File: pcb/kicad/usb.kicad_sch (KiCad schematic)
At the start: 5 parts, among them J1 USB_C_Receptacle_USB2.0, U5 USBLC6-2SC6

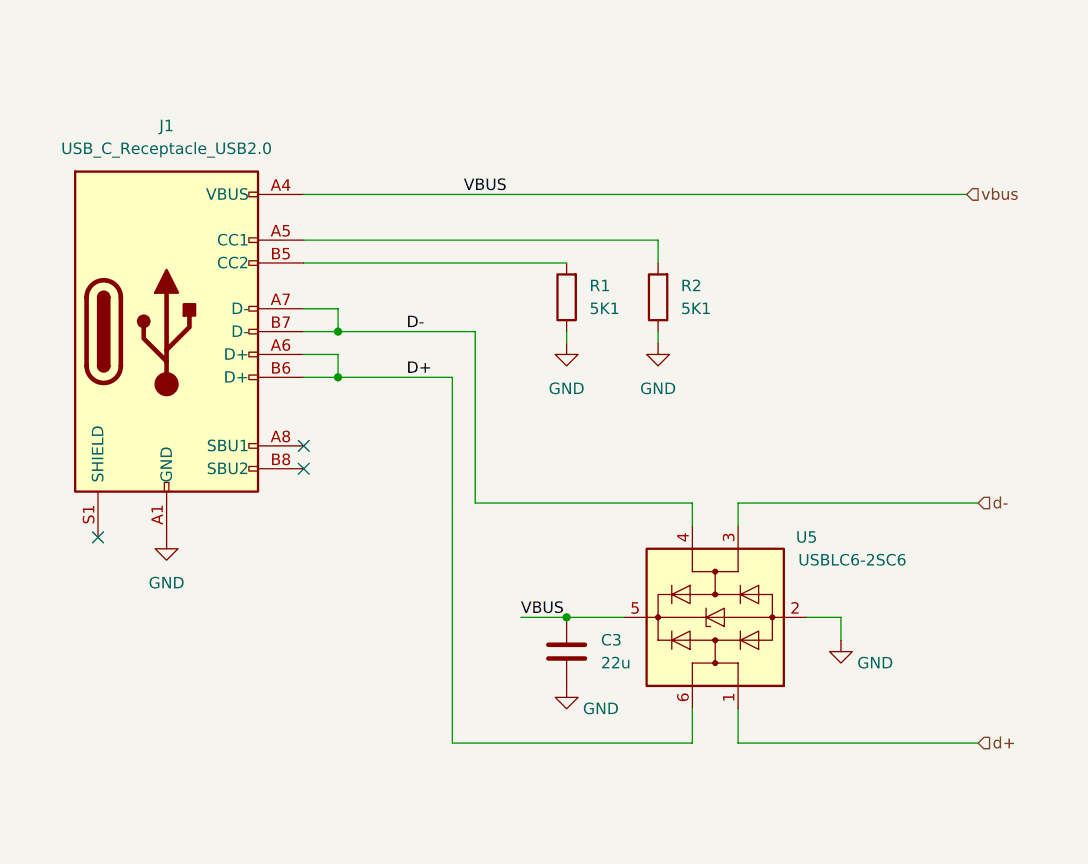
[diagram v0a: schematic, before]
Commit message: Add SoC and pinout.
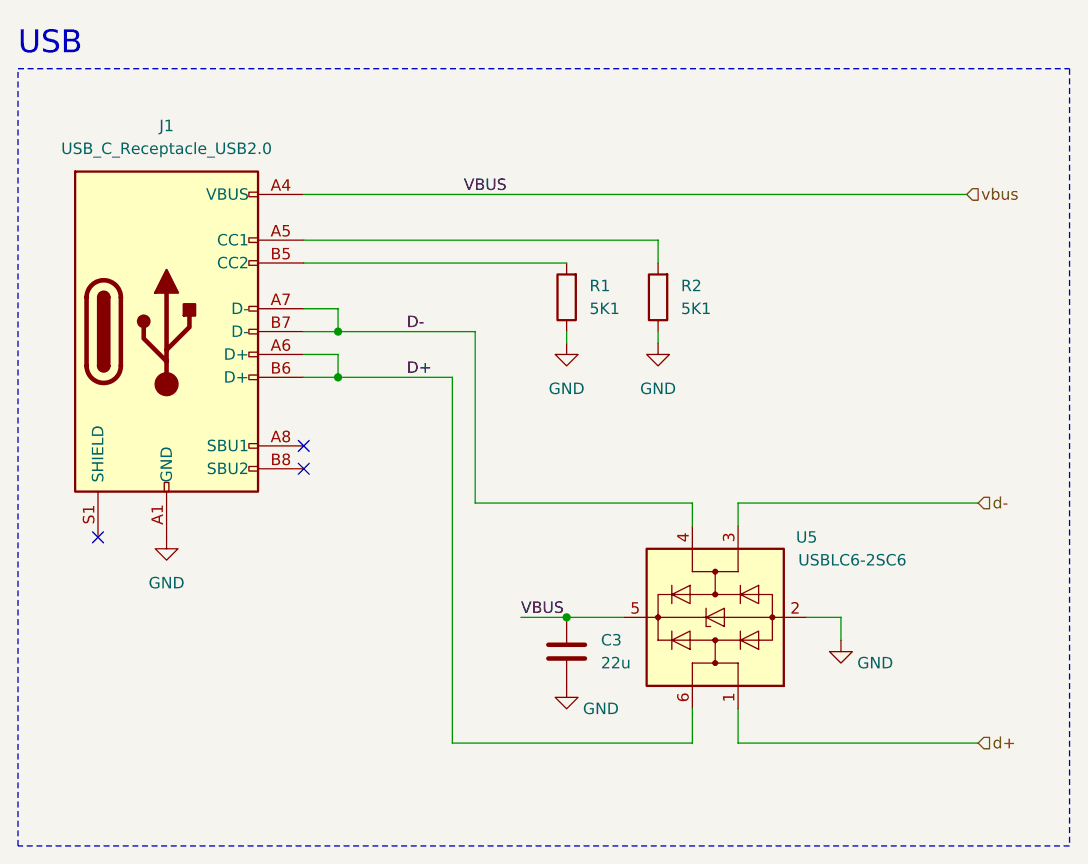
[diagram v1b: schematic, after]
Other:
- note added: "USB"
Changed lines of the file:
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@@
     (stroke (width 0) (type default))
+  )
+  (rectangle (start 88.9 55.88) (end 205.74 142.24)
+    (stroke (width 0) (type dash))
+    (fill (type none))
+  )
+  (text "USB" (at 88.9 54.61 0)
+    (effects (font (size 2.54 2.54)) (justify left bottom))
   )
   (label "D+" (at 132.08 90.17 0) (fields_autoplaced)

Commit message: Added converters, controls and updated annotations.
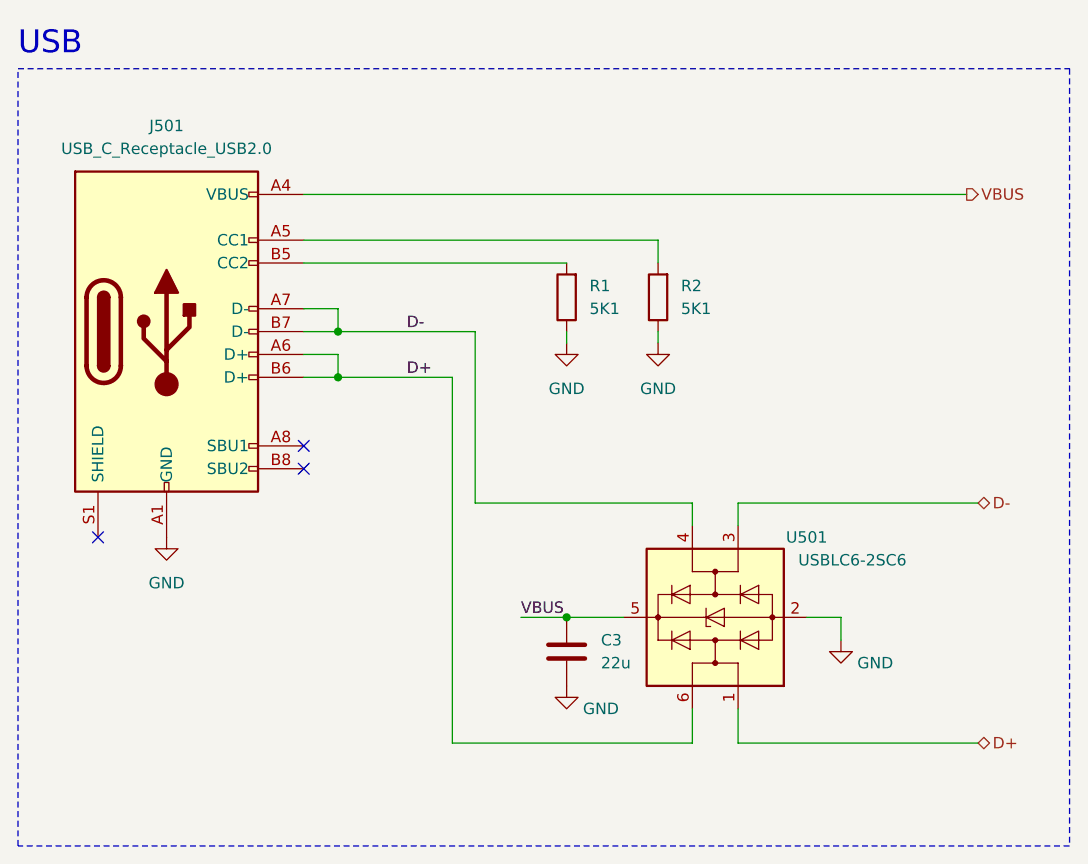
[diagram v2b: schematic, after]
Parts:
- removed J1: USB_C_Receptacle_USB2.0, symbol Connector:USB_C_Receptacle_USB2.0
- added J501: USB_C_Receptacle_USB2.0, symbol Connector:USB_C_Receptacle_USB2.0
- renumbered U5 to U501
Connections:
- net d+ is gone; now on net D+: U501.1 (I/O1)
- net d- is gone; now on net D-: U501.3 (I/O2)
- net D+: now also J501.A6 (D+), J501.B6 (D+)
- net D-: now also J501.A7 (D-), J501.B7 (D-)
- net GND: now also J501.A1 (GND), J501.A12 (GND), J501.B1 (GND), J501.B12 (GND)
- net at R2.2: now also J501.A5 (CC1)
- net at R1.2: now also J501.B5 (CC2)
- net vbus renamed VBUS
- net VBUS: now also J501.A4 (VBUS), J501.A9 (VBUS), J501.B4 (VBUS), J501.B9 (VBUS)
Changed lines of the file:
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@@
-    (effects (font (size 1.27 1.27)) (justify left bottom))
-  )
-  (label "VBUS" (at 138.43 69.85 0) (fields_autoplaced)
     (effects (font (size 1.27 1.27)) (justify left bottom))
   )
@@
     (effects (font (size 1.27 1.27)) (justify left bottom))
   )
-  (hierarchical_label "vbus" (shape input) (at 194.31 69.85 0) (fields_autoplaced)
+  (hierarchical_label "VBUS" (shape output) (at 194.31 69.85 0) (fields_autoplaced)
     (effects (font (size 1.27 1.27)) (justify left))
   )
-  (hierarchical_label "d-" (shape input) (at 195.58 104.14 0) (fields_autoplaced)
+  (hierarchical_label "D-" (shape bidirectional) (at 195.58 104.14 0) (fields_autoplaced)
     (effects (font (size 1.27 1.27)) (justify left))
   )
-  (hierarchical_label "d+" (shape input) (at 195.58 130.81 0) (fields_autoplaced)
+  (hierarchical_label "D+" (shape bidirectional) (at 195.58 130.81 0) (fields_autoplaced)
     (effects (font (size 1.27 1.27)) (justify left))
   )
-  (symbol (lib_id "Device:C") (at 149.86 120.65 0) (unit 1)
-    (in_bom yes) (on_board yes) (dnp no) (fields_autoplaced)
-    (property "Reference" "C3" (at 153.67 119.38 0)
-      (effects (font (size 1.27 1.27)) (justify left))
-    )
-    (property "Value" "22u" (at 153.67 121.92 0)
-      (effects (font (size 1.27 1.27)) (justify left))
-    )
-    (property "Footprint" "Capacitor_SMD:C_0805_2012Metric" (at 150.8252 124.46 0)
-      (effects (font (size 1.27 1.27)) hide)
-    )
-    (property "Datasheet" "~" (at 149.86 120.65 0)
-      (effects (font (size 1.27 1.27)) hide)
-    )
-    (pin "1")
-    (pin "2")
-    (instances
-      (project "guitar-pedal"
-        (path "/aeca30b5-691d-475f-a243-a02c48b6690c/87d54cf0-3e2a-4f61-ade7-69dbca04292f"
-          (reference "C3") (unit 1)
-        )
-        (path "/aeca30b5-691d-475f-a243-a02c48b6690c/59bf6d34-53a6-42d0-b8a6-f9cf82e6ba67"
-          (reference "C17") (unit 1)
-        )
-      )
-    )
-  )
-  (symbol (lib_id "power:GND") (at 180.34 119.38 0) (unit 1)
-    (in_bom yes) (on_board yes) (dnp no)
-    (property "Reference" "#PWR02" (at 180.34 125.73 0)
-      (effects (font (size 1.27 1.27)) hide)
-    )
-    (property "Value" "GND" (at 184.15 121.92 0)
-      (effects (font (size 1.27 1.27)))
-    )
-    (property "Footprint" "" (at 180.34 119.38 0)
-      (effects (font (size 1.27 1.27)) hide)
-    )
-    (property "Datasheet" "" (at 180.34 119.38 0)
-      (effects (font (size 1.27 1.27)) hide)
-    )
-    (pin "1")
-    (instances
-      (project "guitar-pedal"
-        (path "/aeca30b5-691d-475f-a243-a02c48b6690c"
-          (reference "#PWR02") (unit 1)
-        )
-        (path "/aeca30b5-691d-475f-a243-a02c48b6690c/59bf6d34-53a6-42d0-b8a6-f9cf82e6ba67"
-          (reference "#PWR024") (unit 1)
-        )
-      )
-    )
-  )
-  (symbol (lib_id "power:GND") (at 105.41 107.95 0) (unit 1)
-    (in_bom yes) (on_board yes) (dnp no) (fields_autoplaced)
-    (property "Reference" "#PWR01" (at 105.41 114.3 0)
-      (effects (font (size 1.27 1.27)) hide)
-    )
-    (property "Value" "GND" (at 105.41 113.03 0)
-      (effects (font (size 1.27 1.27)))
-    )
-    (property "Footprint" "" (at 105.41 107.95 0)
-      (effects (font (size 1.27 1.27)) hide)
-    )
-    (property "Datasheet" "" (at 105.41 107.95 0)
-      (effects (font (size 1.27 1.27)) hide)
-    )
-    (pin "1")
-    (instances
-      (project "guitar-pedal"
-        (path "/aeca30b5-691d-475f-a243-a02c48b6690c"
-          (reference "#PWR01") (unit 1)
-        )
-        (path "/aeca30b5-691d-475f-a243-a02c48b6690c/59bf6d34-53a6-42d0-b8a6-f9cf82e6ba67"
-          (reference "#PWR01") (unit 1)
-        )
-      )
-    )
-  )
   (symbol (lib_id "Connector:USB_C_Receptacle_USB2.0") (at 105.41 85.09 0) (unit 1)
     (in_bom yes) (on_board yes) (dnp no) (fields_autoplaced)
-    (property "Reference" "J1" (at 105.41 62.23 0)
+    (property "Reference" "J501" (at 105.41 62.23 0)
       (effects (font (size 1.27 1.27)))
     )
@@
     (instances
       (project "guitar-pedal"
-        (path "/aeca30b5-691d-475f-a243-a02c48b6690c"
-          (reference "J1") (unit 1)
-        )
-        (path "/aeca30b5-691d-475f-a243-a02c48b6690c/59bf6d34-53a6-42d0-b8a6-f9cf82e6ba67"
-          (reference "J1") (unit 1)
+        (path "/aeca30b5-691d-475f-a243-a02c48b6690c/59bf6d34-53a6-42d0-b8a6-f9cf82e6ba67"
+          (reference "J501") (unit 1)
+        )
+      )
+    )
+  )
+  (symbol (lib_id "Device:C") (at 149.86 120.65 0) (unit 1)
+    (in_bom yes) (on_board yes) (dnp no) (fields_autoplaced)
+    (property "Reference" "C3" (at 153.67 119.38 0)
+      (effects (font (size 1.27 1.27)) (justify left))
+    )
+    (property "Value" "22u" (at 153.67 121.92 0)
+      (effects (font (size 1.27 1.27)) (justify left))
+    )
+    (property "Footprint" "Capacitor_SMD:C_0805_2012Metric" (at 150.8252 124.46 0)
+      (effects (font (size 1.27 1.27)) hide)
+    )
+    (property "Datasheet" "~" (at 149.86 120.65 0)
+      (effects (font (size 1.27 1.27)) hide)
+    )
+    (pin "1")
+    (pin "2")
+    (instances
+      (project "guitar-pedal"
+        (path "/aeca30b5-691d-475f-a243-a02c48b6690c/87d54cf0-3e2a-4f61-ade7-69dbca04292f"
+          (reference "C3") (unit 1)
+        )
+        (path "/aeca30b5-691d-475f-a243-a02c48b6690c/59bf6d34-53a6-42d0-b8a6-f9cf82e6ba67"
+          (reference "C501") (unit 1)
+        )
+      )
+    )
+  )
+  (symbol (lib_id "power:GND") (at 180.34 119.38 0) (unit 1)
+    (in_bom yes) (on_board yes) (dnp no)
+    (property "Reference" "#PWR02" (at 180.34 125.73 0)
+      (effects (font (size 1.27 1.27)) hide)
+    )
+    (property "Value" "GND" (at 184.15 121.92 0)
+      (effects (font (size 1.27 1.27)))
+    )
+    (property "Footprint" "" (at 180.34 119.38 0)
+      (effects (font (size 1.27 1.27)) hide)
+    )
+    (property "Datasheet" "" (at 180.34 119.38 0)
+      (effects (font (size 1.27 1.27)) hide)
+    )
+    (pin "1")
+    (instances
+      (project "guitar-pedal"
+        (path "/aeca30b5-691d-475f-a243-a02c48b6690c"
+          (reference "#PWR02") (unit 1)
+        )
+        (path "/aeca30b5-691d-475f-a243-a02c48b6690c/59bf6d34-53a6-42d0-b8a6-f9cf82e6ba67"
+          (reference "#PWR0505") (unit 1)
+        )
+      )
+    )
+  )
+  (symbol (lib_id "power:GND") (at 105.41 107.95 0) (unit 1)
+    (in_bom yes) (on_board yes) (dnp no) (fields_autoplaced)
+    (property "Reference" "#PWR01" (at 105.41 114.3 0)
+      (effects (font (size 1.27 1.27)) hide)
+    )
+    (property "Value" "GND" (at 105.41 113.03 0)
+      (effects (font (size 1.27 1.27)))
+    )
+    (property "Footprint" "" (at 105.41 107.95 0)
+      (effects (font (size 1.27 1.27)) hide)
+    )
+    (property "Datasheet" "" (at 105.41 107.95 0)
+      (effects (font (size 1.27 1.27)) hide)
+    )
+    (pin "1")
+    (instances
+      (project "guitar-pedal"
+        (path "/aeca30b5-691d-475f-a243-a02c48b6690c"
+          (reference "#PWR01") (unit 1)
+        )
+        (path "/aeca30b5-691d-475f-a243-a02c48b6690c/59bf6d34-53a6-42d0-b8a6-f9cf82e6ba67"
+          (reference "#PWR0501") (unit 1)
         )
       )
@@
         )
         (path "/aeca30b5-691d-475f-a243-a02c48b6690c/59bf6d34-53a6-42d0-b8a6-f9cf82e6ba67"
-          (reference "#PWR02") (unit 1)
+          (reference "#PWR0502") (unit 1)
         )
       )
@@
         )
         (path "/aeca30b5-691d-475f-a243-a02c48b6690c/59bf6d34-53a6-42d0-b8a6-f9cf82e6ba67"
-          (reference "#PWR023") (unit 1)
+          (reference "#PWR0503") (unit 1)
         )
       )
@@
         )
         (path "/aeca30b5-691d-475f-a243-a02c48b6690c/59bf6d34-53a6-42d0-b8a6-f9cf82e6ba67"
-          (reference "#PWR03") (unit 1)
+          (reference "#PWR0504") (unit 1)
         )
       )
@@
         )
         (path "/aeca30b5-691d-475f-a243-a02c48b6690c/59bf6d34-53a6-42d0-b8a6-f9cf82e6ba67"
-          (reference "R2") (unit 1)
+          (reference "R502") (unit 1)
         )
       )
@@
   (symbol (lib_id "Power_Protection:USBLC6-2SC6") (at 166.37 116.84 90) (unit 1)
     (in_bom yes) (on_board yes) (dnp no)
-    (property "Reference" "U5" (at 176.53 107.95 90)
+    (property "Reference" "U501" (at 176.53 107.95 90)
       (effects (font (size 1.27 1.27)))
     )
@@
       (project "guitar-pedal"
         (path "/aeca30b5-691d-475f-a243-a02c48b6690c/59bf6d34-53a6-42d0-b8a6-f9cf82e6ba67"
-          (reference "U5") (unit 1)
+          (reference "U501") (unit 1)
         )
       )
@@
         )
         (path "/aeca30b5-691d-475f-a243-a02c48b6690c/59bf6d34-53a6-42d0-b8a6-f9cf82e6ba67"
-          (reference "R1") (unit 1)
-        )
-      )
+          (reference "R501") (unit 1)
+        )
+      )

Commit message: Added PCB layout and fabrication output.
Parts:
- J501: value USB_C_Receptacle_USB2.0 -> USB4105-GF-A; footprint (none) -> Connector_USB:USB_C_Receptacle_GCT_USB4105-xx-A_16P_TopMnt_Horizontal
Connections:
- net D+: no longer J501.A6 (D+), J501.B6 (D+), U501.6 (I/O1)
- net D-: no longer J501.A7 (D-), J501.B7 (D-), U501.4 (I/O2)
- new net CONN_D+: J501.A6 (D+), J501.B6 (D+), U501.6 (I/O1)
- new net CONN_D-: J501.A7 (D-), J501.B7 (D-), U501.4 (I/O2)
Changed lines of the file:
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@@
+    (stroke (width 0) (type default))
+  )
+  (wire (pts (xy 124.46 90.17) (xy 137.16 90.17))
     (stroke (width 0) (type default))
   )
@@
     (stroke (width 0) (type default))
   )
+  (wire (pts (xy 124.46 85.09) (xy 139.7 85.09))
+    (stroke (width 0) (type default))
+  )
   (wire (pts (xy 144.78 116.84) (xy 149.86 116.84))
     (stroke (width 0) (type default))
@@
     (stroke (width 0) (type default))
   )
-  (wire (pts (xy 124.46 85.09) (xy 139.7 85.09))
-    (stroke (width 0) (type default))
-  )
   (wire (pts (xy 176.53 116.84) (xy 180.34 116.84))
     (stroke (width 0) (type default))
@@
   )
   (wire (pts (xy 120.65 69.85) (xy 194.31 69.85))
-    (stroke (width 0) (type default))
-  )
-  (wire (pts (xy 124.46 90.17) (xy 137.16 90.17))
     (stroke (width 0) (type default))
   )
@@
     (effects (font (size 2.54 2.54)) (justify left bottom))
   )
-  (label "D+" (at 132.08 90.17 0) (fields_autoplaced)
+  (label "CONN_D+" (at 128.27 90.17 0) (fields_autoplaced)
     (effects (font (size 1.27 1.27)) (justify left bottom))
   )
-  (label "D-" (at 132.08 85.09 0) (fields_autoplaced)
+  (label "CONN_D-" (at 128.27 85.09 0) (fields_autoplaced)
     (effects (font (size 1.27 1.27)) (justify left bottom))
   )
@@
       (effects (font (size 1.27 1.27)))
     )
-    (property "Value" "USB_C_Receptacle_USB2.0" (at 105.41 64.77 0)
+    (property "Value" "USB4105-GF-A" (at 105.41 64.77 0)
       (effects (font (size 1.27 1.27)))
     )
-    (property "Footprint" "" (at 109.22 85.09 0)
+    (property "Footprint" "Connector_USB:USB_C_Receptacle_GCT_USB4105-xx-A_16P_TopMnt_Horizontal" (at 109.22 85.09 0)
       (effects (font (size 1.27 1.27)) hide)
     )

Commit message: Add part numbers to components for ordering.
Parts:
- C3: Part Number (none) -> C0805C226M8PAC7210
- J501: Part Number (none) -> USB4105-GF-A; Supplier Link (none) -> https://www.digikey.de/en/products/detail/gct/USB4105-GF-A/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
- R1, R2: Part Number (none) -> RT0805FRE135K1L
- U501: Part Number (none) -> USBLC6-2SC6; Supplier Link (none) -> https://www.digikey.de/en/products/detail/stmicroelectronic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
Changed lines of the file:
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@@
+      (effects (font (size 1.27 1.27)) hide)
+    )
+    (property "Supplier Link" "https://www.digikey.de/en/products/detail/gct/USB4105-GF-A/11198441" (at 105.41 85.09 0)
+      (effects (font (size 1.27 1.27)) hide)
+    )
+    (property "Part Number" "USB4105-GF-A" (at 105.41 85.09 0)
       (effects (font (size 1.27 1.27)) hide)
     )
@@
       (effects (font (size 1.27 1.27)) hide)
     )
+    (property "Supplier Link" "" (at 149.86 120.65 0)
+      (effects (font (size 1.27 1.27)) hide)
+    )
+    (property "Part Number" "C0805C226M8PAC7210" (at 149.86 120.65 0)
+      (effects (font (size 1.27 1.27)) hide)
+    )
     (pin "1")
     (pin "2")
@@
       (effects (font (size 1.27 1.27)) hide)
     )
+    (property "Supplier Link" "" (at 160.02 81.28 0)
+      (effects (font (size 1.27 1.27)) hide)
+    )
+    (property "Part Number" "RT0805FRE135K1L" (at 160.02 81.28 0)
+      (effects (font (size 1.27 1.27)) hide)
+    )
     (pin "1")
     (pin "2")
@@
     )
     (property "Datasheet" "https://www.st.com/resource/en/datasheet/usblc6-2.pdf" (at 157.48 111.76 0)
+      (effects (font (size 1.27 1.27)) hide)
+    )
+    (property "Part Number" "USBLC6-2SC6" (at 166.37 116.84 0)
+      (effects (font (size 1.27 1.27)) hide)
+    )
+    (property "Supplier Link" "https://www.digikey.de/en/products/detail/stmicroelectronics/USBLC6-2SC6/1040559" (at 166.37 116.84 0)
       (effects (font (size 1.27 1.27)) hide)
     )
@@
       (effects (font (size 1.27 1.27)) hide)
     )
+    (property "Supplier Link" "" (at 149.86 81.28 0)
+      (effects (font (size 1.27 1.27)) hide)
+    )
+    (property "Part Number" "RT0805FRE135K1L" (at 149.86 81.28 0)
+      (effects (font (size 1.27 1.27)) hide)
+    )
